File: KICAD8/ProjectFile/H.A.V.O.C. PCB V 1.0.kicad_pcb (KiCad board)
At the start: 8 copper layers, 65 x 100 mm, 129 parts, among them IC2 STM32H755IIT6, J10 Conn_02x10_Top_Bottom, J2 USB_B_Micro, J3 XT60-M, J5 Conn_Coaxial, J6 Conn_Coaxial, J7 Conn_02x10_Top_Bottom, M1 SERVO1, M2 SERVO2, M3 SERVO3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

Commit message: Testing Commit
Added a single GND via in a random area (No trace overlaps)
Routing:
- net GND: vias 120 -> 121
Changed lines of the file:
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@@
+	)
+	(via
+		(at 179.35 142.79)
+		(size 0.8)
+		(drill 0.4)
+		(layers "F.Cu" "B.Cu")
+		(free yes)
+		(net 2)
 	)
 	(via

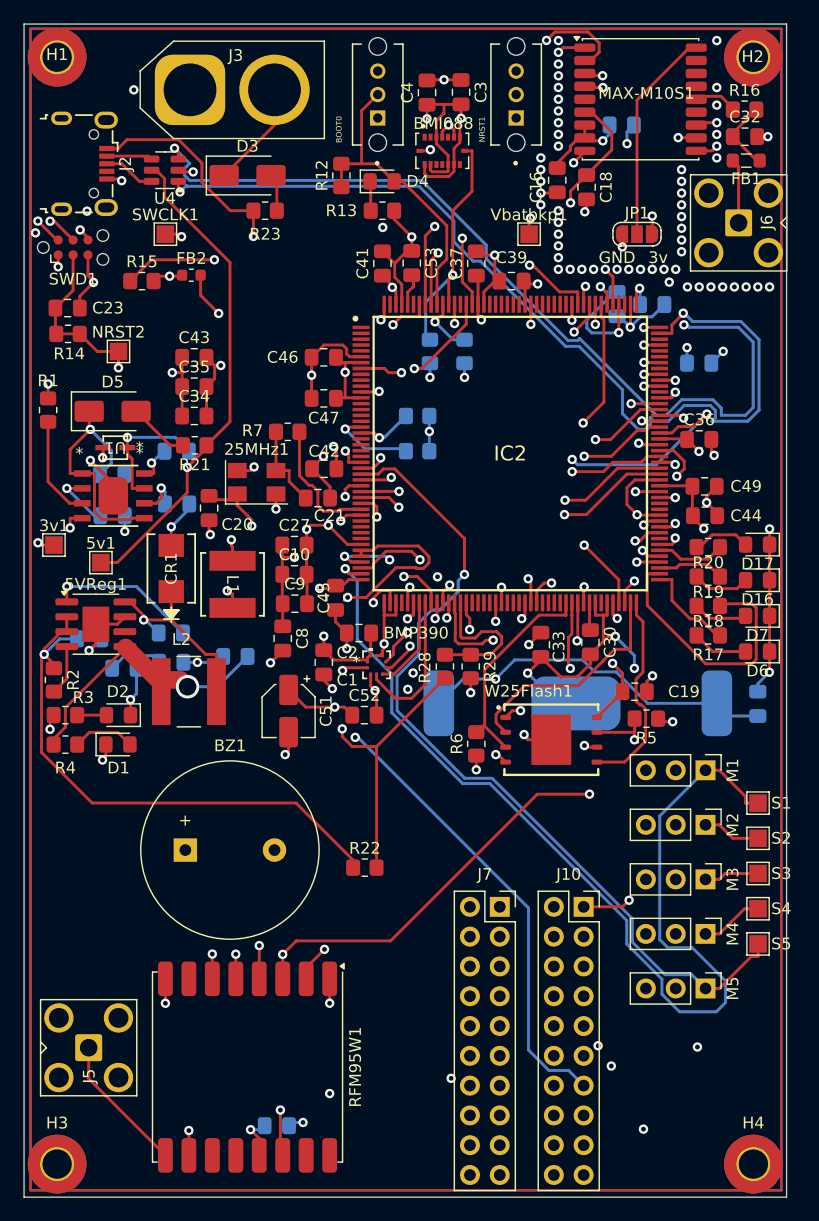
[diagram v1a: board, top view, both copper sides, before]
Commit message: Deep dived through every net class ensuring everything was connected. Optimized a few paths that were unecessarily long.
2 suggestions. I would have a second pair of eyes look over the ground and power connections again. There are just so many and are so small.

Suggestion 2: More like a question, should we make the traces for VBat thicker? Considering its a power trace
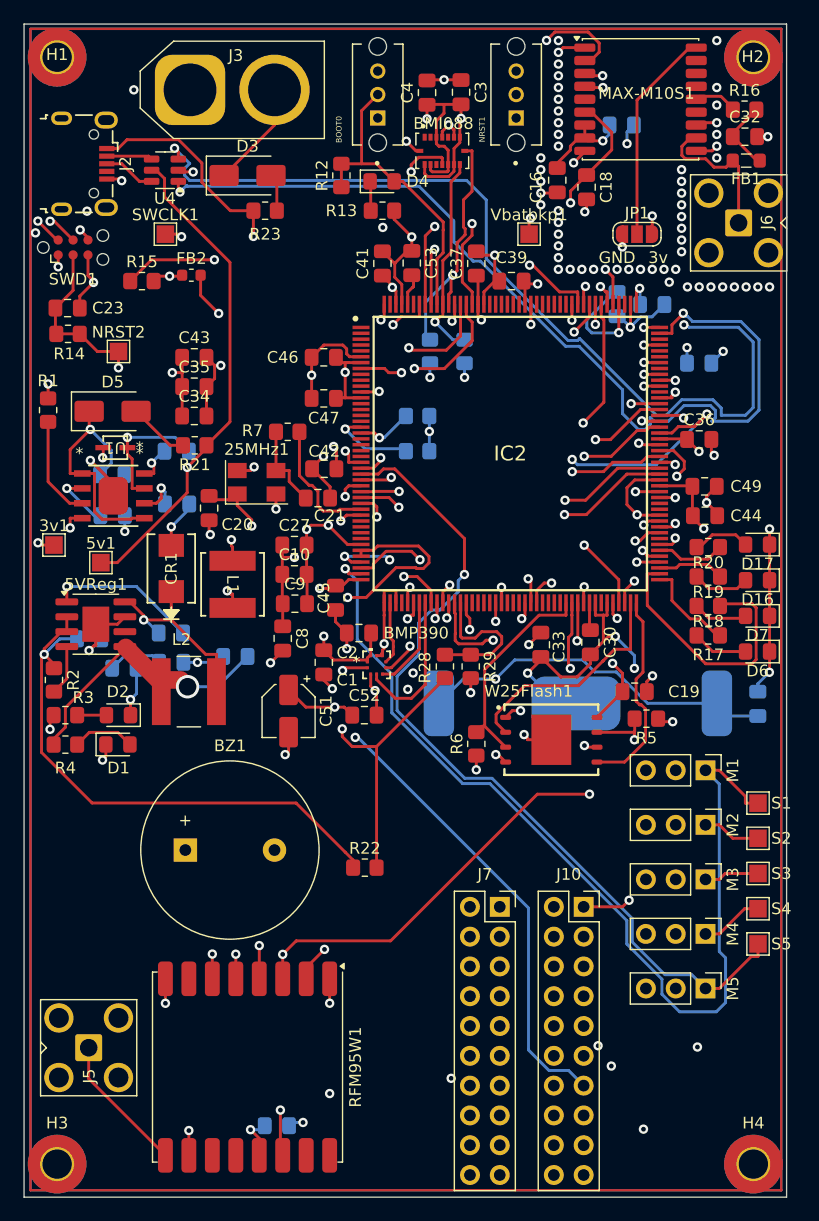
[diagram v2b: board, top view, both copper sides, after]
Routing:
- net INT_GYR: track 0.00 -> 27.9 mm, vias 0 -> 2
- net I2C1_SDA: track 5.06 -> 17.6 mm
- net GP_GPIO10: track 45.9 -> 38.4 mm, vias 2 -> 1
- net SPI1_INT: track 10.4 -> 5.42 mm, vias 2 -> 0
- net SERVO1: track 87.7 -> 83.3 mm
- net INT_ACC: track 19.9 -> 24.0 mm
- net Net-(J6-In): track 16.6 -> 12.8 mm, vias 1 -> 0
- net GP_GPIO34: track 91.2 -> 94.3 mm
- net NRST: track 77.2 -> 79.7 mm
- net USB_D-: track 75.7 -> 77.9 mm
- net SWO: track 43.5 -> 45.1 mm
- net GND: track 222.0 -> 223.0 mm

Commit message: Review of Changes
Looked over and fixed connections throughout the board, specifically the power/gnd connections.
Vbat traces made thicker -> 1 mm wide where necessary(not to LED/analog voltage measure)

Advise to review again-break into sections
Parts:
- moved R22 36.0 mm to (125.0, 102.6)
- moved J6 0.37 mm to (182.5, 72.5)
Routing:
- net Net-(5VReg1-EN): track 48.6 -> 15.0 mm
- net GND: track 223.0 -> 250.2 mm, vias 121 -> 168
- net USB_D-: track 77.9 -> 91.3 mm
- net USB_D+: track 81.4 -> 88.0 mm
- net VBAT: track 122.4 -> 127.2 mm, vias 2 -> 5
- net +5V: track 185.7 -> 189.7 mm
- net +3V3: track 144.9 -> 148.2 mm
- net UART5_TX: track 57.9 -> 57.1 mm
- net Net-(5VReg1-PGOOD): track 4.30 -> 5.10 mm
- net Net-(5VReg1-BST): track 12.9 -> 12.1 mm
- net SPI3_MOSI: vias 3 -> 2

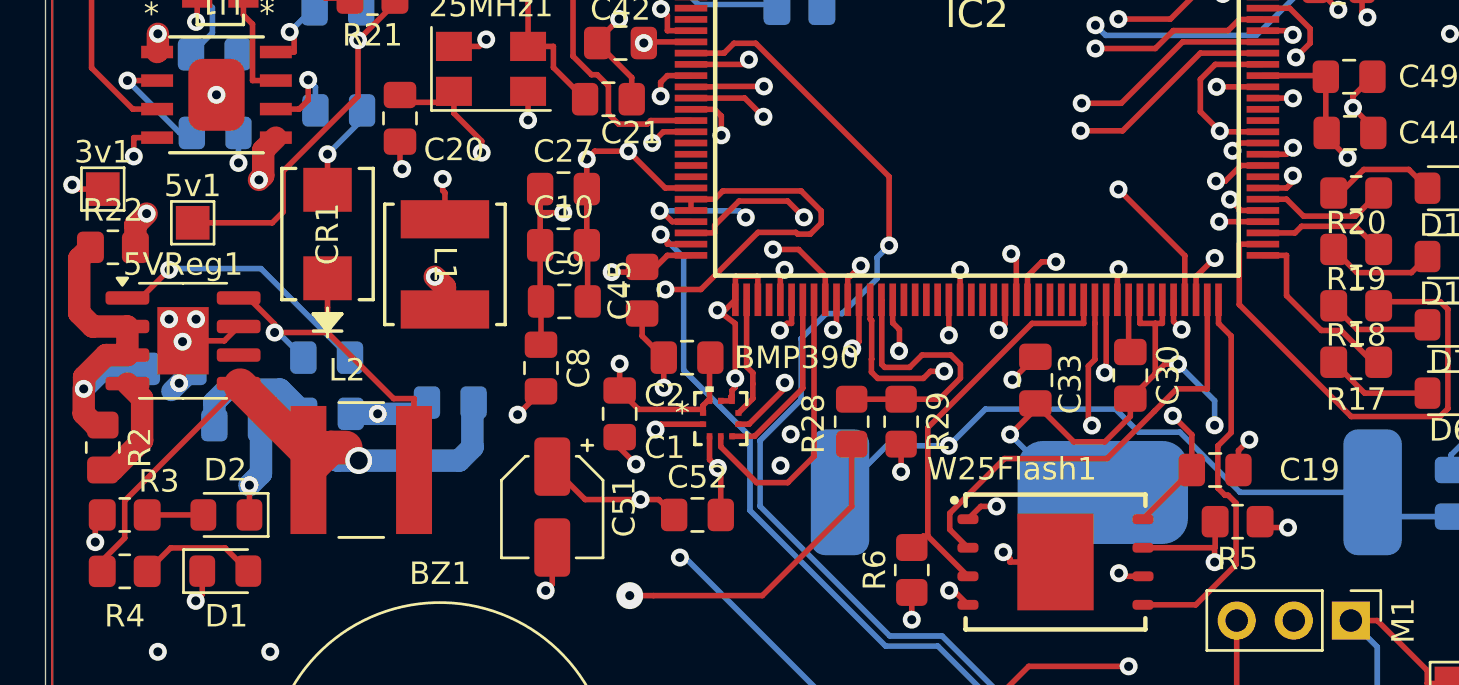
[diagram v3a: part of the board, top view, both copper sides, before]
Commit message: Minor changes
Removed some right angles for traces, changed 5V trace width
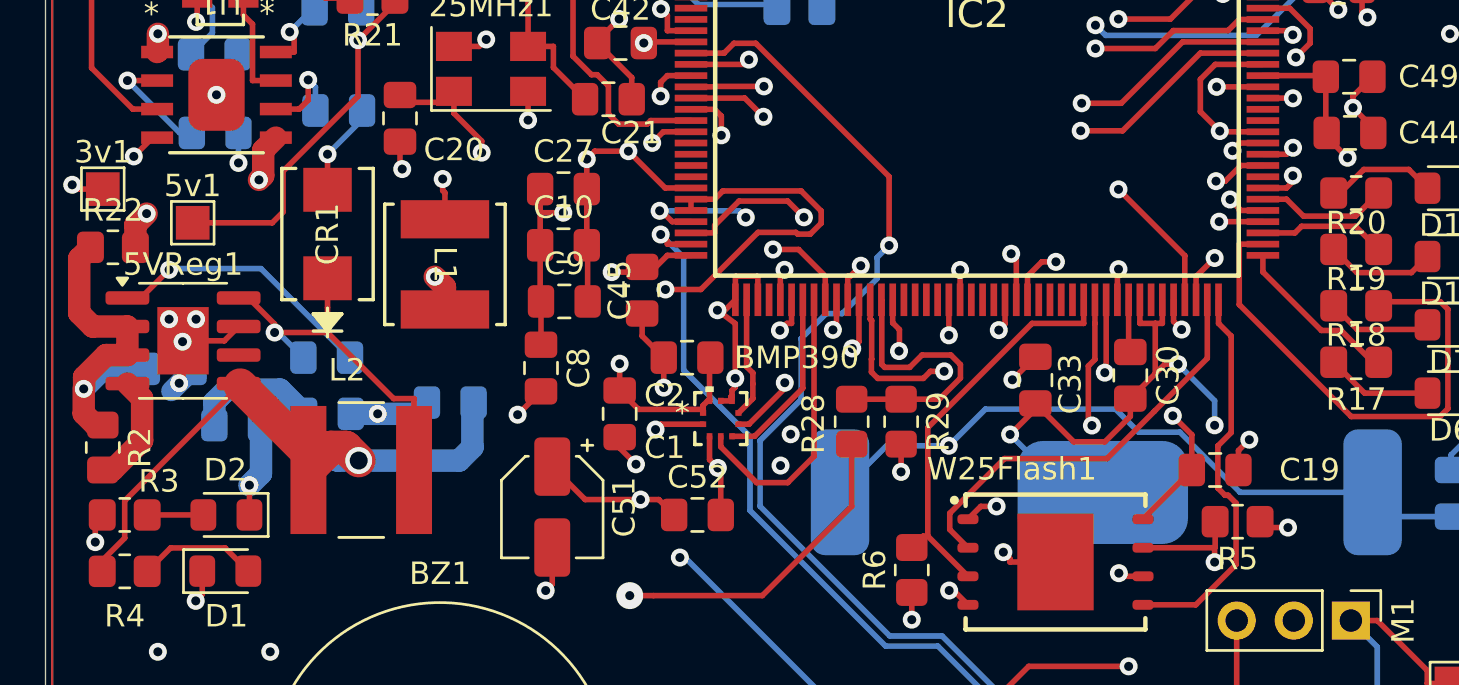
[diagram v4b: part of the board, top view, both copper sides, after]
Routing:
- net SPI2_MISO: track 19.6 -> 18.8 mm
- net LED1: track 8.17 -> 7.55 mm
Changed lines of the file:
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@@
 	)
 	(segment
-		(start 125.8789 98.5449)
-		(end 125.8789 97.71)
-		(width 0.25)
-		(layer "F.Cu")
-		(net 2)
-	)
-	(segment
 		(start 147.5125 82.95)
 		(end 146.4625 84)
@@
 	)
 	(segment
-		(start 125.879 98.545)
-		(end 125.8789 98.5449)
+		(start 125.8789 98.5449)
+		(end 126.7138 97.71)
 		(width 0.25)
 		(layer "F.Cu")
@@
 	)
 	(segment
+		(start 125.879 98.545)
+		(end 125.8789 98.5449)
+		(width 0.25)
+		(layer "F.Cu")
+		(net 2)
+	)
+	(segment
 		(start 174.96 133.15)
 		(end 174.96 137.8)
@@
 	)
 	(segment
-		(start 126.9168 97.71)
-		(end 125.8789 97.71)
-		(width 0.25)
-		(layer "F.Cu")
-		(net 2)
-	)
-	(segment
 		(start 129.91 106.75)
 		(end 130.545 106.115)
@@
 	)
 	(segment
+		(start 126.7138 97.71)
+		(end 126.9168 97.71)
+		(width 0.25)
+		(layer "F.Cu")
+		(net 2)
+	)
+	(segment
 		(start 174.96 128.5)
 		(end 174.96 130.78)
@@
 		(start 135.309 111.5)
 		(end 135.888 112.079)
-		(width 0.25)
+		(width 1.5)
 		(layer "F.Cu")
 		(net 4)
@@
 	)
 	(segment
-		(start 128.2 83.5)
-		(end 126.7 82)
-		(width 0.25)
-		(layer "F.Cu")
-		(net 71)
-	)
-	(segment
 		(start 124.625 81.925)
 		(end 124.625 79.8)
@@
 	)
 	(segment
-		(start 130 83.5)
-		(end 128.2 83.5)
+		(start 126.13 75.27)
+		(end 126.13 78.295)
 		(width 0.25)
 		(layer "F.Cu")
@@
 	)
 	(segment
-		(start 126.13 75.27)
-		(end 126.13 78.295)
+		(start 130 83.5)
+		(end 128.2 83.5)
 		(width 0.25)
 		(layer "F.Cu")
@@
 		(net 71)
 	)
+	(segment
+		(start 128.2 83.5)
+		(end 126.7 82)
+		(width 0.25)
+		(layer "F.Cu")
+		(net 71)
+	)
 	(via
 		(at 130 84.8918)
@@
 	)
 	(segment
-		(start 181.019 107.705)
-		(end 181.275 107.705)
-		(width 0.25)
-		(layer "F.Cu")
-		(net 94)
-	)
-	(segment
-		(start 178.728 106.2907)
-		(end 179.6047 106.2907)
+		(start 179.6047 106.2907)
+		(end 181.019 107.705)
 		(width 0.25)
 		(layer "F.Cu")
@@
 	)
 	(segment
-		(start 176.125 102.95)
-		(end 177.1767 102.95)
+		(start 181.019 107.705)
+		(end 181.275 107.705)
 		(width 0.25)
 		(layer "F.Cu")
@@
 	)
 	(segment
-		(start 177.1767 102.95)
-		(end 177.1767 104.7394)
+		(start 178.728 106.2907)
+		(end 179.6047 106.2907)
 		(width 0.25)
 		(layer "F.Cu")
@@
 	)
 	(segment
-		(start 179.6047 106.2907)
-		(end 181.019 107.705)
+		(start 176.125 102.95)
+		(end 176.125 103.6877)
 		(width 0.25)
 		(layer "F.Cu")
@@
 	)
 	(segment
-		(start 177.1767 104.7394)
+		(start 176.125 103.6877)
 		(end 178.728 106.2907)
 		(width 0.25)
@@
 	)
 	(segment
-		(start 172.289495 108.89)
-		(end 171.3023 109.877195)
-		(width 0.25)
-		(layer "F.Cu")
-		(net 163)
-	)
-	(segment
-		(start 162.1896 115.1496)
-		(end 163 115.96)
+		(start 162.1896 114.4261)
+		(end 164.6238 111.9919)
 		(width 0.25)
 		(layer "F.Cu")
@@
 	)
 	(segment
-		(start 171.3023 109.8803)
-		(end 169.1907 111.9919)
+		(start 169.1907 111.9919)
+		(end 171.3023 109.8803)
 		(width 0.25)
 		(layer "F.Cu")
@@
 	)
 	(segment
-		(start 169.1907 111.9919)
-		(end 164.6238 111.9919)
+		(start 171.3023 109.877195)
+		(end 173.65 107.529495)
 		(width 0.25)
 		(layer "F.Cu")
@@
 	)
 	(segment
-		(start 171.3023 109.877195)
-		(end 171.3023 109.8803)
+		(start 173.65 107.529495)
+		(end 173.65 104.925)
 		(width 0.25)
 		(layer "F.Cu")
@@
 	)
 	(segment
-		(start 162.1896 114.4261)
+		(start 163 115.96)
 		(end 162.1896 115.1496)
 		(width 0.25)
@@
 	)
 	(segment
-		(start 173.65 104.925)
-		(end 173.65 108.89)
+		(start 164.6238 111.9919)
+		(end 169.1907 111.9919)
 		(width 0.25)
 		(layer "F.Cu")
@@
 	)
 	(segment
-		(start 173.65 108.89)
-		(end 172.289495 108.89)
+		(start 162.1896 115.1496)
+		(end 162.1896 114.4261)
 		(width 0.25)
 		(layer "F.Cu")
@@
 	)
 	(segment
-		(start 164.6238 111.9919)
-		(end 162.1896 114.4261)
+		(start 171.3023 109.8803)
+		(end 171.3023 109.877195)
 		(width 0.25)
 		(layer "F.Cu")
